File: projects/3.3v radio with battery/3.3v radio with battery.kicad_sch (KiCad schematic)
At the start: 9 parts, among them J1 USB_B

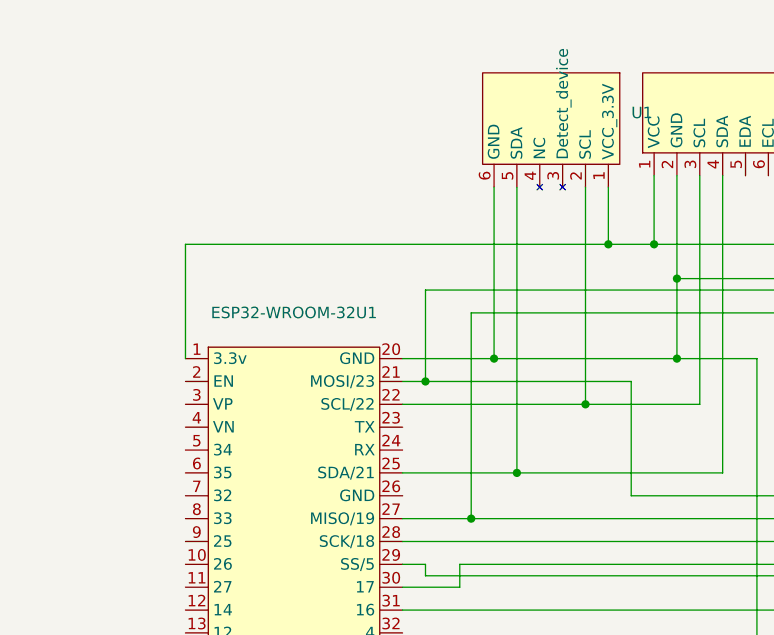
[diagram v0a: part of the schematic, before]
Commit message: update 3.3v rad
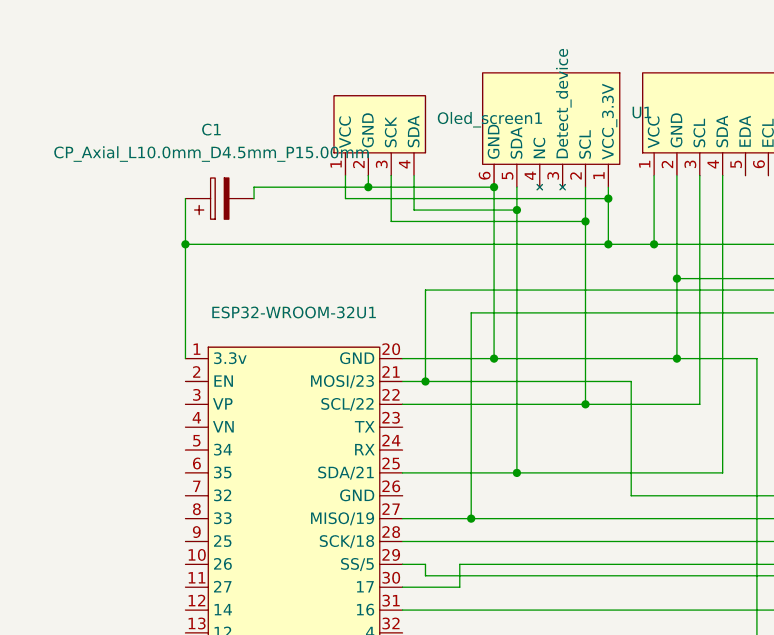
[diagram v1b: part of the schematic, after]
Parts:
- added C1: CP_Axial_L10.0mm_D4.5mm_P15.00mm, Capacitor_THT:CP_Radial_D8.0mm_P3.50mm, symbol PCM_Capacitor_AKL:CP_Axial_L10.0mm_D4.5mm_P15.00mm
- added Oled_screen1: ~, Connector_PinHeader_2.54mm:PinHeader_1x04_P2.54mm_Horizontal, symbol Symbols_cez:1.3/0.91_inch_Oled_screen
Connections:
- net at ESP32-WROOM-32U1.20 (GND), MPU1.2 (GND), NRF1.1 (GND)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: now also C1.2, Oled_screen1.2 (GND)
- net at ESP32-WROOM-32U1.1 (3.3v), MPU1.1 (VCC), NRF1.2 (VCC)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: now also C1.1, Oled_screen1.1 (VCC)
- net at ESP32-WROOM-32U1.22 (SCL/22), MPU1.3 (SCL), U1.2 (SCL): now also Oled_screen1.3 (SCK)
- net at ESP32-WROOM-32U1.25 (SDA/21), MPU1.4 (SDA), U1.5 (SDA): now also Oled_screen1.4 (SDA)

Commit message: a lot of project updates
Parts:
- added C2, C3: CP_Axial_L10.0mm_D4.5mm_P15.00mm, Capacitor_THT:CP_Radial_D8.0mm_P3.50mm, symbol PCM_Capacitor_AKL:CP_Axial_L10.0mm_D4.5mm_P15.00mm
- added TP1: TestPoint, Connector_PinHeader_2.54mm:PinHeader_1x01_P2.54mm_Vertical, symbol Connector:TestPoint
- added U6: ~, Footprints_cez:Switch A03 PS-22F03, symbol Symbols_cez:Switch_A03_PS-22F03
- U5: footprint Connector_PinHeader_2.54mm:PinHeader_1x02_P2.54mm_Vertical -> Footprints_cez:BH-18650-PC2
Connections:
- net at C1.2, ESP32-WROOM-32U1.20 (GND), MPU1.2 (GND)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: now also C2.2, C3.2
- net at C1.1, ESP32-WROOM-32U1.1 (3.3v), MPU1.1 (VCC)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: now also C2.1, C3.1
- net at U3.5 (GND_IN), U4.3 (GND): now also U6.2 (no)
- new net: TP1.1, U3.7 (ON/OFF), U6.4 (nc)

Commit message: only multi remote left
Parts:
- added GPS1: ~, Footprints_cez:GY-NEO6MV2_flipped, symbol Symbols_cez:GY-NEO6MV2
- added U7: ~, Footprints_cez:BME280, symbol Symbols_cez:BME280_3.3V
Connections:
- net at C1.2, C2.2, C3.2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: now also ESP32-WROOM-32U1.14 (GND), GPS1.1 (GND), U7.2 (GND); no longer ESP32-WROOM-32U1.20 (GND)
- net at C1.1, C2.1, C3.1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: now also GPS1.4 (VCC), U7.1 (VCC)
- net at NRF1.3 (CE): now also ESP32-WROOM-32U1.7 (32); no longer ESP32-WROOM-32U1.31 (16)
- net at NRF1.4 (~{CSN}): now also ESP32-WROOM-32U1.8 (33); no longer ESP32-WROOM-32U1.30 (17)
- net at ESP32-WROOM-32U1.22 (SCL/22), MPU1.3 (SCL), Oled_screen1.3 (SCK)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: now also U7.3 (SCL)
- net at ESP32-WROOM-32U1.25 (SDA/21), MPU1.4 (SDA), Oled_screen1.4 (SDA)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: now also U7.4 (SDA)
- new net: ESP32-WROOM-32U1.31 (RX2/16), GPS1.2 (TX)
- new net: ESP32-WROOM-32U1.30 (TX2/17), GPS1.3 (RX)
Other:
- moved on the sheet: J1, TP1, U3, U4, U5, U6
